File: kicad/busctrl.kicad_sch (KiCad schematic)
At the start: 6 parts, among them J1 VLB_slot, U1 74LS244, U2 27C020

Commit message: changed QFP and ROM footprint
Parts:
- U2: footprint Package_DIP:DIP-32_W15.24mm -> VLB:EEPROM_combo
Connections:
- net ISA_D4: now also U1.2 (I0a); no longer U1.8 (I3a)
- net ISA_D5: now also U1.4 (I1a); no longer U1.6 (I2a)
- net ISA_D6: now also U1.6 (I2a); no longer U1.4 (I1a)
- net ISA_D7: now also U1.8 (I3a); no longer U1.2 (I0a)
- net R_D4: now also U1.18 (O0a); no longer U1.12 (O3a)
- net R_D5: now also U1.16 (O1a); no longer U1.14 (O2a)
- net R_D6: now also U1.14 (O2a); no longer U1.16 (O1a)
- net R_D7: now also U1.12 (O3a); no longer U1.18 (O0a)
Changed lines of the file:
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@@
-    (effects (font (size 1.27 1.27)) (justify left bottom))
-  )
-  (label "ISA_D7" (at 49.53 69.85 0) (fields_autoplaced)
     (effects (font (size 1.27 1.27)) (justify left bottom))
   )
@@
     (effects (font (size 1.27 1.27)) (justify right bottom))
   )
+  (label "R_D4" (at 90.17 69.85 180) (fields_autoplaced)
+    (effects (font (size 1.27 1.27)) (justify right bottom))
+  )
   (label "ISA_D2" (at 49.53 82.55 0) (fields_autoplaced)
     (effects (font (size 1.27 1.27)) (justify left bottom))
@@
     (effects (font (size 1.27 1.27)) (justify right bottom))
   )
-  (label "R_D4" (at 90.17 77.47 180) (fields_autoplaced)
-    (effects (font (size 1.27 1.27)) (justify right bottom))
-  )
   (label "R_D7" (at 137.16 85.09 180) (fields_autoplaced)
     (effects (font (size 1.27 1.27)) (justify right bottom))
@@
     (effects (font (size 1.27 1.27)) (justify right bottom))
   )
+  (label "ISA_D4" (at 49.53 69.85 0) (fields_autoplaced)
+    (effects (font (size 1.27 1.27)) (justify left bottom))
+  )
   (label "ISA_D0" (at 49.53 87.63 0) (fields_autoplaced)
     (effects (font (size 1.27 1.27)) (justify left bottom))
@@
     (effects (font (size 1.27 1.27)) (justify right bottom))
   )
-  (label "R_D7" (at 90.17 69.85 180) (fields_autoplaced)
+  (label "R_D5" (at 90.17 72.39 180) (fields_autoplaced)
     (effects (font (size 1.27 1.27)) (justify right bottom))
   )
@@
     (effects (font (size 1.27 1.27)) (justify left bottom))
   )
-  (label "R_D6" (at 90.17 72.39 180) (fields_autoplaced)
+  (label "R_D6" (at 90.17 74.93 180) (fields_autoplaced)
     (effects (font (size 1.27 1.27)) (justify right bottom))
   )
@@
     (effects (font (size 1.27 1.27)) (justify left bottom))
   )
+  (label "ISA_D5" (at 49.53 72.39 0) (fields_autoplaced)
+    (effects (font (size 1.27 1.27)) (justify left bottom))
+  )
   (label "R_A13" (at 102.87 100.33 0) (fields_autoplaced)
     (effects (font (size 1.27 1.27)) (justify left bottom))
   )
-  (label "ISA_D4" (at 49.53 77.47 0) (fields_autoplaced)
-    (effects (font (size 1.27 1.27)) (justify left bottom))
-  )
-  (label "R_D5" (at 90.17 74.93 180) (fields_autoplaced)
-    (effects (font (size 1.27 1.27)) (justify right bottom))
+  (label "ISA_D6" (at 49.53 74.93 0) (fields_autoplaced)
+    (effects (font (size 1.27 1.27)) (justify left bottom))
   )
   (label "R_A14" (at 102.87 102.87 0) (fields_autoplaced)
     (effects (font (size 1.27 1.27)) (justify left bottom))
   )
-  (label "ISA_D6" (at 49.53 72.39 0) (fields_autoplaced)
-    (effects (font (size 1.27 1.27)) (justify left bottom))
-  )
   (label "R_A8" (at 203.2 116.84 180) (fields_autoplaced)
     (effects (font (size 1.27 1.27)) (justify right bottom))
@@
     (effects (font (size 1.27 1.27)) (justify right bottom))
   )
-  (label "ISA_D5" (at 49.53 74.93 0) (fields_autoplaced)
-    (effects (font (size 1.27 1.27)) (justify left bottom))
-  )
   (label "R_A10" (at 102.87 92.71 0) (fields_autoplaced)
     (effects (font (size 1.27 1.27)) (justify left bottom))
@@
   (label "R_A5" (at 203.2 124.46 180) (fields_autoplaced)
     (effects (font (size 1.27 1.27)) (justify right bottom))
+  )
+  (label "R_D7" (at 90.17 77.47 180) (fields_autoplaced)
+    (effects (font (size 1.27 1.27)) (justify right bottom))
+  )
+  (label "ISA_D7" (at 49.53 77.47 0) (fields_autoplaced)
+    (effects (font (size 1.27 1.27)) (justify left bottom))
   )
   (label "R_A7" (at 102.87 85.09 0) (fields_autoplaced)
@@
       (effects (font (size 1.27 1.27)) (justify left))
     )
-    (property "Footprint" "Package_DIP:DIP-32_W15.24mm" (at 119.38 95.25 0)
-      (effects (font (size 1.27 1.27)) hide)
-    )
+    (property "Footprint" "VLB:EEPROM_combo" (at 119.38 95.25 0)
+      (effects (font (size 1.27 1.27)) hide)
+    )

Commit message: some improvements here and there
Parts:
- added C20: 100nF, Capacitor_SMD:C_0805_2012Metric_Pad1.18x1.45mm_HandSolder, symbol Device:C
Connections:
- net GND: now also C20.1
- net VCC: now also C20.2
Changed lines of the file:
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@@
+    )
+  )
+  (symbol (lib_id "power:VCC") (at 107.95 53.34 0) (unit 1)
+    (in_bom yes) (on_board yes) (dnp no) (fields_autoplaced)
+    (property "Reference" "#PWR026" (at 107.95 57.15 0)
+      (effects (font (size 1.27 1.27)) hide)
+    )
+    (property "Value" "VCC" (at 107.95 49.53 0)
+      (effects (font (size 1.27 1.27)))
+    )
+    (property "Footprint" "" (at 107.95 53.34 0)
+      (effects (font (size 1.27 1.27)) hide)
+    )
+    (property "Datasheet" "" (at 107.95 53.34 0)
+      (effects (font (size 1.27 1.27)) hide)
+    )
+    (pin "1")
+    (instances
+      (project "virge-vlb"
+        (path "/e8216711-86b5-4276-82f4-4c7ed22b9a9c"
+          (reference "#PWR026") (unit 1)
+        )
+        (path "/e8216711-86b5-4276-82f4-4c7ed22b9a9c/485e825d-a3d2-4e3d-9ea7-d005dd511bf5"
+          (reference "#PWR044") (unit 1)
+        )
+      )
     )
   )
@@
         (path "/e8216711-86b5-4276-82f4-4c7ed22b9a9c/485e825d-a3d2-4e3d-9ea7-d005dd511bf5"
           (reference "U1") (unit 1)
+        )
+      )
+    )
+  )
+  (symbol (lib_id "Device:C") (at 107.95 57.15 180) (unit 1)
+    (in_bom yes) (on_board yes) (dnp no)
+    (property "Reference" "C20" (at 105.41 58.42 0)
+      (effects (font (size 1.27 1.27)) (justify left))
+    )
+    (property "Value" "100nF" (at 105.41 54.61 0)
+      (effects (font (size 1.27 1.27)) (justify left))
+    )
+    (property "Footprint" "Capacitor_SMD:C_0805_2012Metric_Pad1.18x1.45mm_HandSolder" (at 106.9848 53.34 0)
+      (effects (font (size 1.27 1.27)) hide)
+    )
+    (property "Datasheet" "~" (at 107.95 57.15 0)
+      (effects (font (size 1.27 1.27)) hide)
+    )
+    (pin "1")
+    (pin "2")
+    (instances
+      (project "virge-vlb"
+        (path "/e8216711-86b5-4276-82f4-4c7ed22b9a9c"
+          (reference "C20") (unit 1)
+        )
+        (path "/e8216711-86b5-4276-82f4-4c7ed22b9a9c/9321f466-5ac6-411a-b039-07fb7f0cdeaa"
+          (reference "C18") (unit 1)
+        )
+        (path "/e8216711-86b5-4276-82f4-4c7ed22b9a9c/485e825d-a3d2-4e3d-9ea7-d005dd511bf5"
+          (reference "C10") (unit 1)
         )
       )
@@
         )
       )
+    )
+  )
+  (symbol (lib_id "power:GND") (at 107.95 60.96 0) (unit 1)
+    (in_bom yes) (on_board yes) (dnp no)
+    (property "Reference" "#PWR058" (at 107.95 67.31 0)
+      (effects (font (size 1.27 1.27)) hide)
+    )
+    (property "Value" "GND" (at 111.76 63.5 0)
+      (effects (font (size 1.27 1.27)))
+    )
+    (property "Footprint" "" (at 107.95 60.96 0)
+      (effects (font (size 1.27 1.27)) hide)
+    )
+    (property "Datasheet" "" (at 107.95 60.96 0)
+      (effects (font (size 1.27 1.27)) hide)
+    )
+    (pin "1")
+    (instances
+      (project "virge-vlb"
+        (path "/e8216711-86b5-4276-82f4-4c7ed22b9a9c/485e825d-a3d2-4e3d-9ea7-d005dd511bf5"
+          (reference "#PWR058") (unit 1)
+        )
+      )

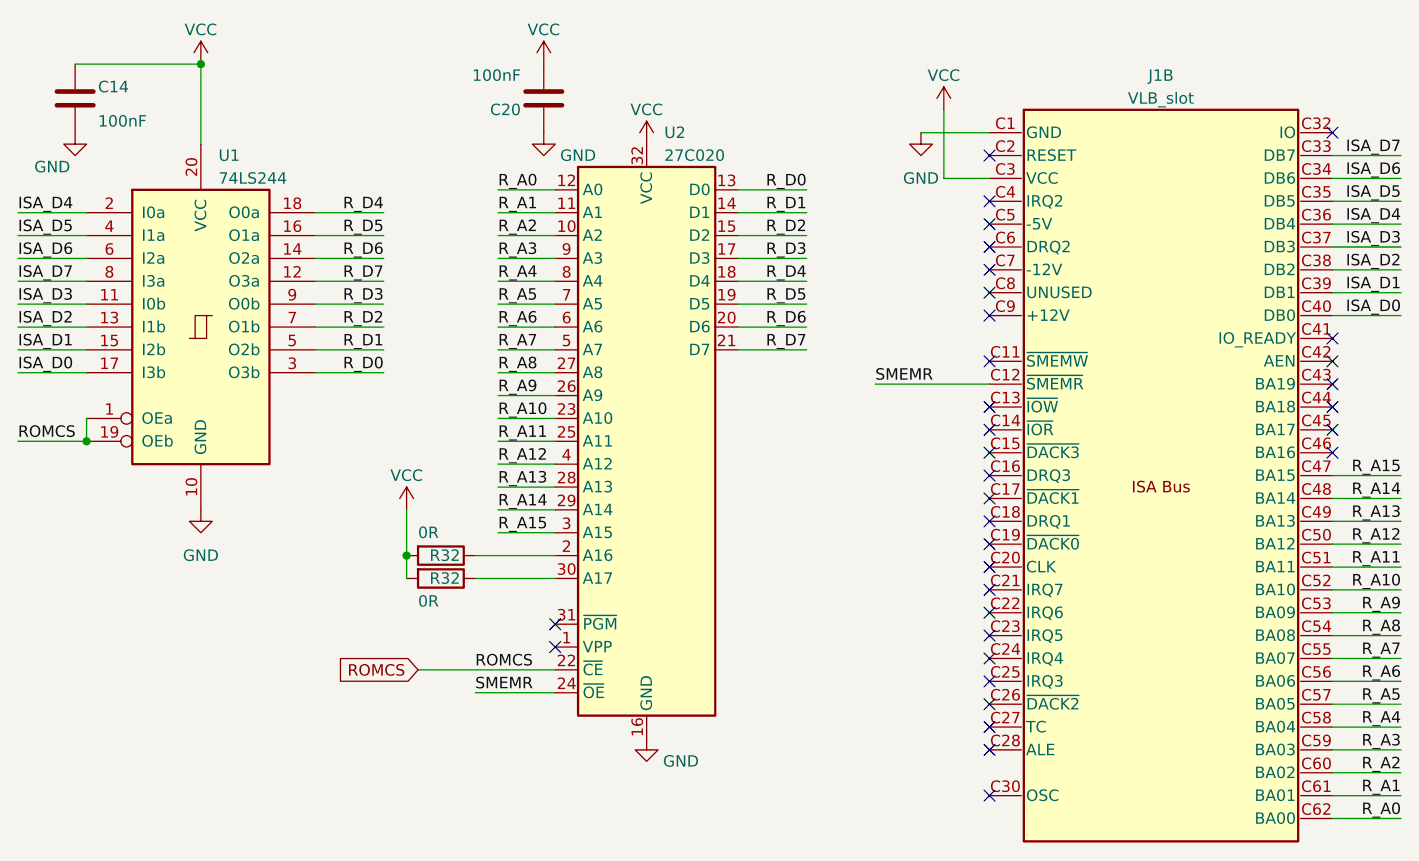
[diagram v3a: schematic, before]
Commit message: some optimizations and silkscreen updating
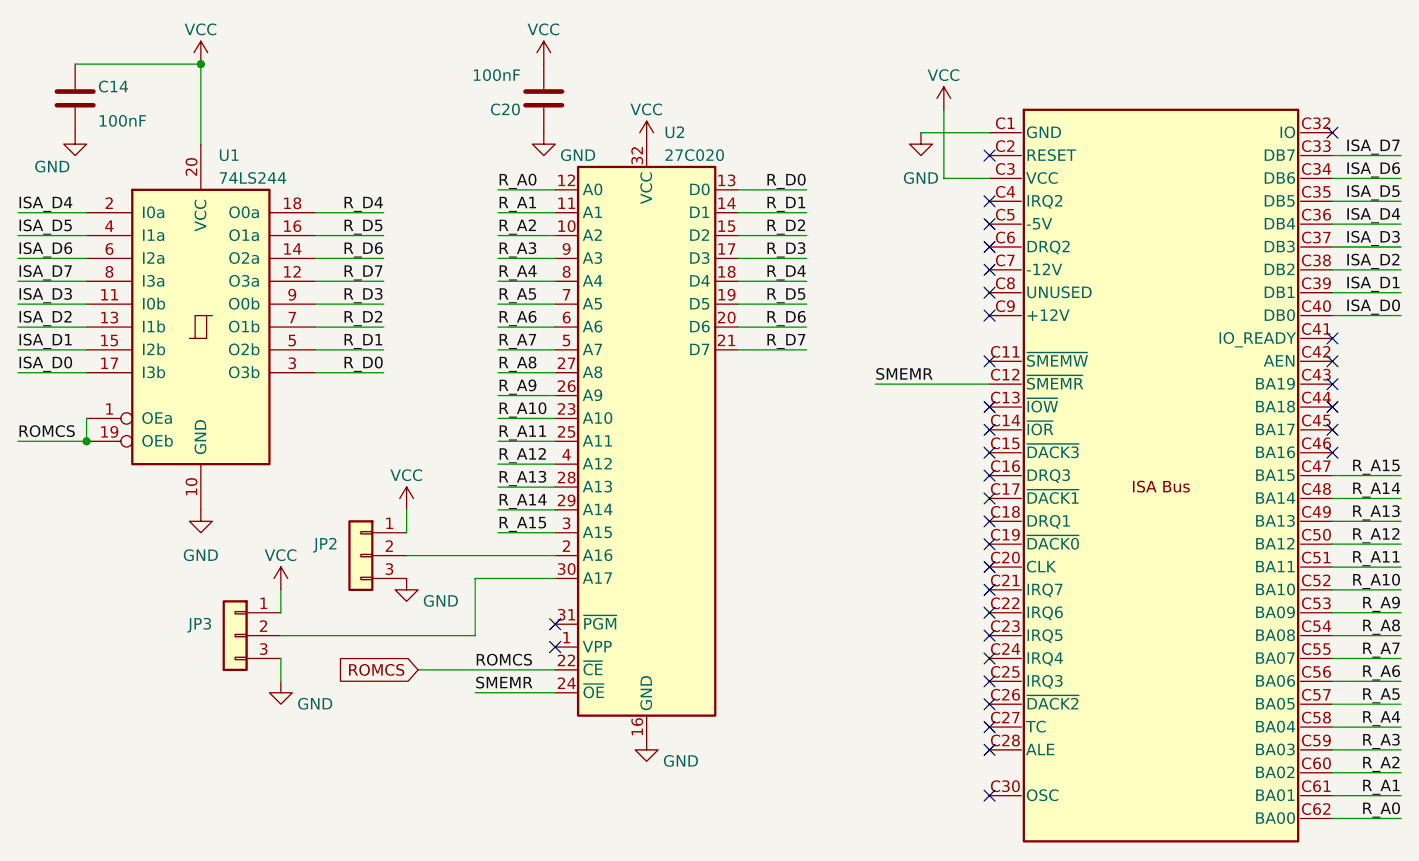
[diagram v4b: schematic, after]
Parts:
- removed R32 (x2): 0R, Resistor_SMD:R_0805_2012Metric_Pad1.20x1.40mm_HandSolder, symbol Device:R
- added JP2, JP3: Conn_01x03, Connector_PinHeader_2.54mm:PinHeader_1x03_P2.54mm_Vertical, symbol Connector_Generic:Conn_01x03
- J1: now left out of the parts list
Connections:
- net GND: now also JP2.3 (Pin_3), JP3.3 (Pin_3)
- net VCC: now also JP2.1 (Pin_1), JP3.1 (Pin_1)
- net at U2.2 (A16): now also JP2.2 (Pin_2)
- net at U2.30 (A17): now also JP3.2 (Pin_2)
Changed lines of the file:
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@@
     (rev "1B")
-  )
-  (junction (at 92.71 107.95) (diameter 0) (color 0 0 0 0)
   )
   (junction (at 57.15 95.25) (diameter 0) (color 0 0 0 0)
@@
     (stroke (width 0) (type default))
   )
-  (wire (pts (xy 100.33 107.95) (xy 109.22 107.95))
+  (wire (pts (xy 92.71 107.95) (xy 109.22 107.95))
     (stroke (width 0) (type default))
   )
@@
     (stroke (width 0) (type default))
   )
+  (wire (pts (xy 78.74 119.38) (xy 78.74 121.92))
+    (stroke (width 0) (type default))
+  )
+  (wire (pts (xy 100.33 116.84) (xy 78.74 116.84))
+    (stroke (width 0) (type default))
+  )
+  (wire (pts (xy 100.33 110.49) (xy 100.33 116.84))
+    (stroke (width 0) (type default))
+  )
+  (wire (pts (xy 78.74 111.76) (xy 78.74 114.3))
+    (stroke (width 0) (type default))
+  )
   (wire (pts (xy 195.58 119.38) (xy 203.2 119.38))
     (stroke (width 0) (type default))
@@
     (stroke (width 0) (type default))
   )
-  (wire (pts (xy 92.71 107.95) (xy 92.71 102.87))
-    (stroke (width 0) (type default))
-  )
   (wire (pts (xy 82.55 82.55) (xy 90.17 82.55))
     (stroke (width 0) (type default))
@@
     (stroke (width 0) (type default))
   )
+  (wire (pts (xy 92.71 102.87) (xy 92.71 105.41))
+    (stroke (width 0) (type default))
+  )
   (wire (pts (xy 144.78 88.9) (xy 157.48 88.9))
     (stroke (width 0) (type default))
@@
   )
   (wire (pts (xy 129.54 82.55) (xy 137.16 82.55))
-    (stroke (width 0) (type default))
-  )
-  (wire (pts (xy 92.71 110.49) (xy 92.71 107.95))
     (stroke (width 0) (type default))
   )
@@
     )
   )
+  (symbol (lib_id "Connector_Generic:Conn_01x03") (at 87.63 107.95 0) (mirror y) (unit 1)
+    (in_bom yes) (on_board yes) (dnp no)
+    (property "Reference" "JP2" (at 85.09 106.68 0)
+      (effects (font (size 1.27 1.27)) (justify left))
+    )
+    (property "Value" "Conn_01x03" (at 85.09 109.22 0)
+      (effects (font (size 1.27 1.27)) (justify left) hide)
+    )
+    (property "Footprint" "Connector_PinHeader_2.54mm:PinHeader_1x03_P2.54mm_Vertical" (at 87.63 107.95 0)
+      (effects (font (size 1.27 1.27)) hide)
+    )
+    (property "Datasheet" "~" (at 87.63 107.95 0)
+      (effects (font (size 1.27 1.27)) hide)
+    )
+    (pin "1")
+    (pin "2")
+    (pin "3")
+    (instances
+      (project "virge-vlb"
+        (path "/e8216711-86b5-4276-82f4-4c7ed22b9a9c/485e825d-a3d2-4e3d-9ea7-d005dd511bf5"
+          (reference "JP2") (unit 1)
+        )
+      )
+    )
+  )
   (symbol (lib_id "power:GND") (at 149.86 60.96 0) (unit 1)
     (in_bom yes) (on_board yes) (dnp no) (fields_autoplaced)
@@
     )
   )
+  (symbol (lib_id "power:GND") (at 92.71 110.49 0) (unit 1)
+    (in_bom yes) (on_board yes) (dnp no)
+    (property "Reference" "#PWR059" (at 92.71 116.84 0)
+      (effects (font (size 1.27 1.27)) hide)
+    )
+    (property "Value" "GND" (at 96.52 113.03 0)
+      (effects (font (size 1.27 1.27)))
+    )
+    (property "Footprint" "" (at 92.71 110.49 0)
+      (effects (font (size 1.27 1.27)) hide)
+    )
+    (property "Datasheet" "" (at 92.71 110.49 0)
+      (effects (font (size 1.27 1.27)) hide)
+    )
+    (pin "1")
+    (instances
+      (project "virge-vlb"
+        (path "/e8216711-86b5-4276-82f4-4c7ed22b9a9c/485e825d-a3d2-4e3d-9ea7-d005dd511bf5"
+          (reference "#PWR059") (unit 1)
+        )
+      )
+    )
+  )
   (symbol (lib_id "power:VCC") (at 107.95 53.34 0) (unit 1)
     (in_bom yes) (on_board yes) (dnp no) (fields_autoplaced)
@@
     )
   )
-  (symbol (lib_id "Device:R") (at 96.52 107.95 270) (unit 1)
+  (symbol (lib_id "Connector_Generic:Conn_01x03") (at 73.66 116.84 0) (mirror y) (unit 1)
     (in_bom yes) (on_board yes) (dnp no)
-    (property "Reference" "R32" (at 95.25 107.95 90)
+    (property "Reference" "JP3" (at 71.12 115.57 0)
       (effects (font (size 1.27 1.27)) (justify left))
     )
-    (property "Value" "0R" (at 93.98 105.41 90)
-      (effects (font (size 1.27 1.27)) (justify left))
-    )
-    (property "Footprint" "Resistor_SMD:R_0805_2012Metric_Pad1.20x1.40mm_HandSolder" (at 96.52 106.172 90)
-      (effects (font (size 1.27 1.27)) hide)
-    )
-    (property "Datasheet" "~" (at 96.52 107.95 0)
+    (property "Value" "Conn_01x03" (at 71.12 118.11 0)
+      (effects (font (size 1.27 1.27)) (justify left) hide)
+    )
+    (property "Footprint" "Connector_PinHeader_2.54mm:PinHeader_1x03_P2.54mm_Vertical" (at 73.66 116.84 0)
+      (effects (font (size 1.27 1.27)) hide)
+    )
+    (property "Datasheet" "~" (at 73.66 116.84 0)
       (effects (font (size 1.27 1.27)) hide)
     )
     (pin "1")
     (pin "2")
-    (instances
-      (project "virge-vlb"
-        (path "/e8216711-86b5-4276-82f4-4c7ed22b9a9c"
-          (reference "R32") (unit 1)
-        )
-        (path "/e8216711-86b5-4276-82f4-4c7ed22b9a9c/73bb2a59-bfac-4efc-8051-53849b0f9066"
-          (reference "R16") (unit 1)
-        )
-        (path "/e8216711-86b5-4276-82f4-4c7ed22b9a9c/485e825d-a3d2-4e3d-9ea7-d005dd511bf5"
-          (reference "R6") (unit 1)
+    (pin "3")
+    (instances
+      (project "virge-vlb"
+        (path "/e8216711-86b5-4276-82f4-4c7ed22b9a9c/485e825d-a3d2-4e3d-9ea7-d005dd511bf5"
+          (reference "JP3") (unit 1)
         )
       )
@@
         (path "/e8216711-86b5-4276-82f4-4c7ed22b9a9c/485e825d-a3d2-4e3d-9ea7-d005dd511bf5"
           (reference "#PWR09") (unit 1)
+        )
+      )
+    )
+  )
+  (symbol (lib_id "power:VCC") (at 78.74 111.76 0) (unit 1)
+    (in_bom yes) (on_board yes) (dnp no) (fields_autoplaced)
+    (property "Reference" "#PWR026" (at 78.74 115.57 0)
+      (effects (font (size 1.27 1.27)) hide)
+    )
+    (property "Value" "VCC" (at 78.74 107.95 0)
+      (effects (font (size 1.27 1.27)))
+    )
+    (property "Footprint" "" (at 78.74 111.76 0)
+      (effects (font (size 1.27 1.27)) hide)
+    )
+    (property "Datasheet" "" (at 78.74 111.76 0)
+      (effects (font (size 1.27 1.27)) hide)
+    )
+    (pin "1")
+    (instances
+      (project "virge-vlb"
+        (path "/e8216711-86b5-4276-82f4-4c7ed22b9a9c"
+          (reference "#PWR026") (unit 1)
+        )
+        (path "/e8216711-86b5-4276-82f4-4c7ed22b9a9c/485e825d-a3d2-4e3d-9ea7-d005dd511bf5"
+          (reference "#PWR061") (unit 1)
         )
       )
@@
   )
   (symbol (lib_id "virge:VLB_slot") (at 175.26 95.25 0) (unit 2)
-    (in_bom yes) (on_board yes) (dnp no) (fields_autoplaced)
+    (in_bom no) (on_board yes) (dnp no) (fields_autoplaced)
     (property "Reference" "J1" (at 176.53 54.61 0)
-      (effects (font (size 1.27 1.27)))
+      (effects (font (size 1.27 1.27)) hide)
     )
     (property "Value" "VLB_slot" (at 176.53 57.15 0)
-      (effects (font (size 1.27 1.27)))
+      (effects (font (size 1.27 1.27)) hide)
     )
     (property "Footprint" "VLB:BUS_VLB_Board" (at 139.7 80.01 0)
@@
     )
   )
+  (symbol (lib_id "power:GND") (at 78.74 121.92 0) (unit 1)
+    (in_bom yes) (on_board yes) (dnp no)
+    (property "Reference" "#PWR060" (at 78.74 128.27 0)
+      (effects (font (size 1.27 1.27)) hide)
+    )
+    (property "Value" "GND" (at 82.55 124.46 0)
+      (effects (font (size 1.27 1.27)))
+    )
+    (property "Footprint" "" (at 78.74 121.92 0)
+      (effects (font (size 1.27 1.27)) hide)
+    )
+    (property "Datasheet" "" (at 78.74 121.92 0)
+      (effects (font (size 1.27 1.27)) hide)
+    )
+    (pin "1")
+    (instances
+      (project "virge-vlb"
+        (path "/e8216711-86b5-4276-82f4-4c7ed22b9a9c/485e825d-a3d2-4e3d-9ea7-d005dd511bf5"
+          (reference "#PWR060") (unit 1)
+        )
+      )
+    )
+  )
   (symbol (lib_id "power:GND") (at 69.85 102.87 0) (unit 1)
     (in_bom yes) (on_board yes) (dnp no) (fields_autoplaced)
@@
         )
       )
-    )
-  )
-  (symbol (lib_id "Device:R") (at 96.52 110.49 270) (unit 1)
-    (in_bom yes) (on_board yes) (dnp no)
-    (property "Reference" "R32" (at 95.25 110.49 90)
-      (effects (font (size 1.27 1.27)) (justify left))
-    )
-    (property "Value" "0R" (at 93.98 113.03 90)
-      (effects (font (size 1.27 1.27)) (justify left))
-    )
-    (property "Footprint" "Resistor_SMD:R_0805_2012Metric_Pad1.20x1.40mm_HandSolder" (at 96.52 108.712 90)
-      (effects (font (size 1.27 1.27)) hide)
-    )
-    (property "Datasheet" "~" (at 96.52 110.49 0)
-      (effects (font (size 1.27 1.27)) hide)
-    )
-    (pin "1")
-    (pin "2")
-    (instances
-      (project "virge-vlb"
-        (path "/e8216711-86b5-4276-82f4-4c7ed22b9a9c"
-          (reference "R32") (unit 1)
-        )
-        (path "/e8216711-86b5-4276-82f4-4c7ed22b9a9c/73bb2a59-bfac-4efc-8051-53849b0f9066"
-          (reference "R16") (unit 1)
-        )
-        (path "/e8216711-86b5-4276-82f4-4c7ed22b9a9c/485e825d-a3d2-4e3d-9ea7-d005dd511bf5"
-          (reference "R7") (unit 1)
-        )
-      )

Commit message: some final tweaks
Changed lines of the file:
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@@
   (symbol (lib_id "Device:C") (at 107.95 57.15 180) (unit 1)
     (in_bom yes) (on_board yes) (dnp no)
-    (property "Reference" "C20" (at 105.41 58.42 0)
+    (property "Reference" "C20" (at 105.41 54.61 0)
       (effects (font (size 1.27 1.27)) (justify left))
     )
-    (property "Value" "100nF" (at 105.41 54.61 0)
+    (property "Value" "100nF" (at 106.68 59.69 0)
       (effects (font (size 1.27 1.27)) (justify left))
     )
@@
         )
         (path "/e8216711-86b5-4276-82f4-4c7ed22b9a9c/485e825d-a3d2-4e3d-9ea7-d005dd511bf5"
-          (reference "C10") (unit 1)
+          (reference "C20") (unit 1)
         )
       )
